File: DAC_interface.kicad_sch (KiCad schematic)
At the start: 8 parts

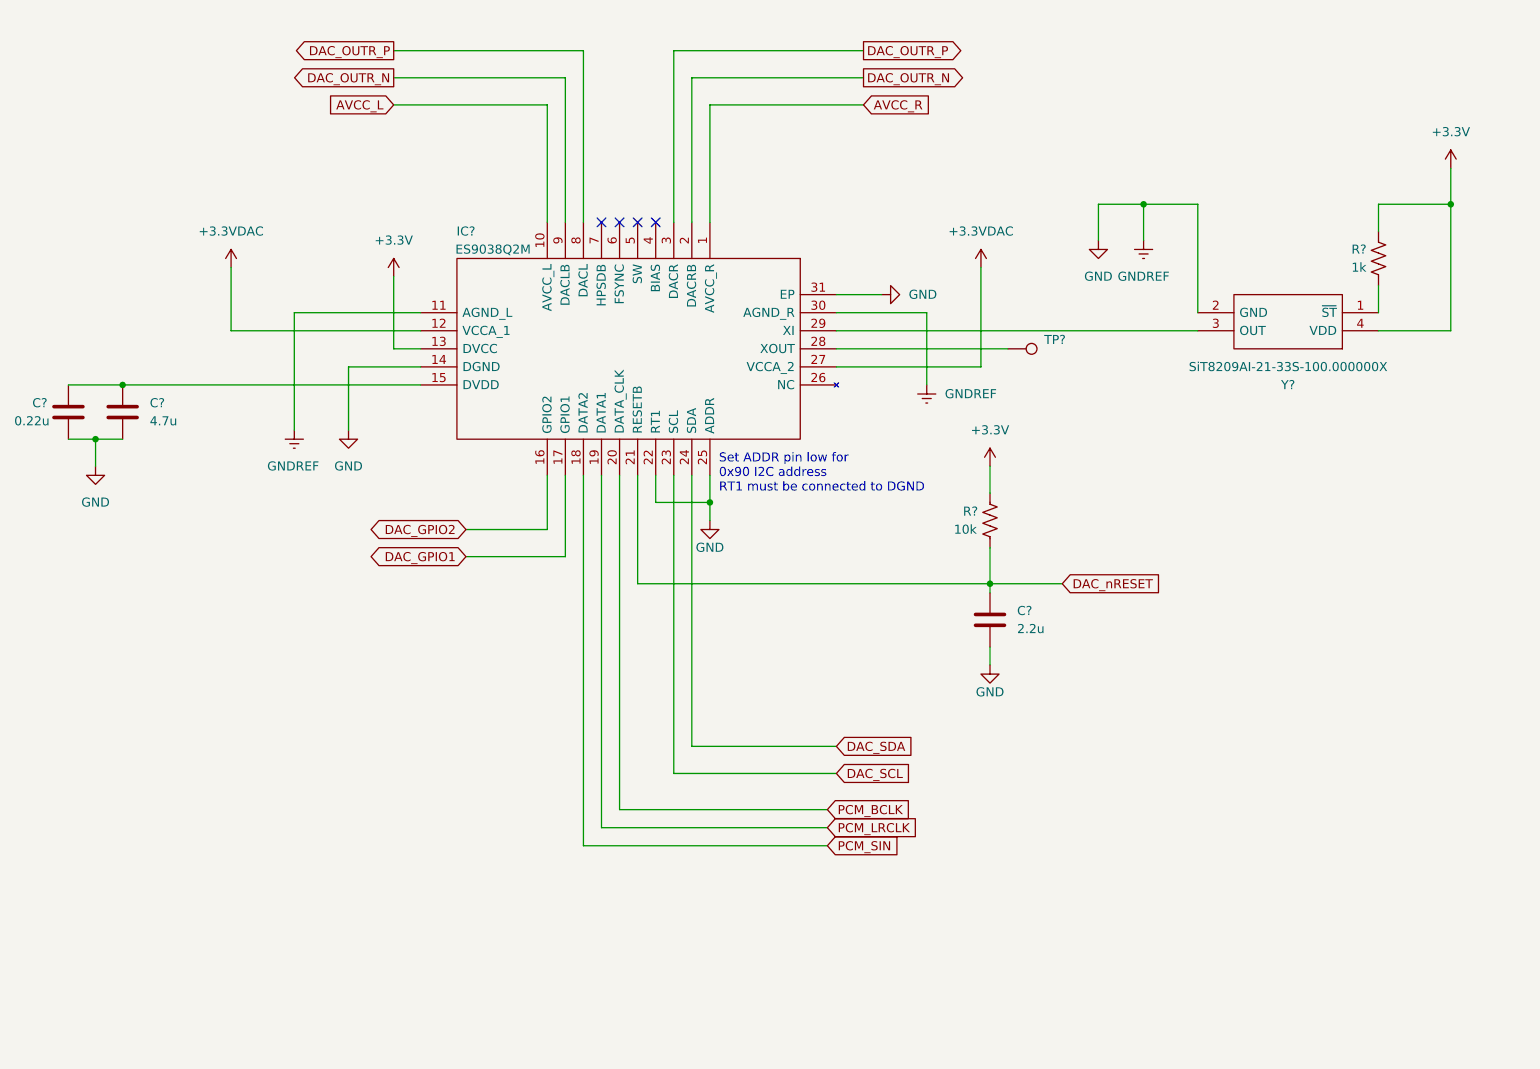
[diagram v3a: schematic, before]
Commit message: Finishing Schematic. Fixed ERC errors
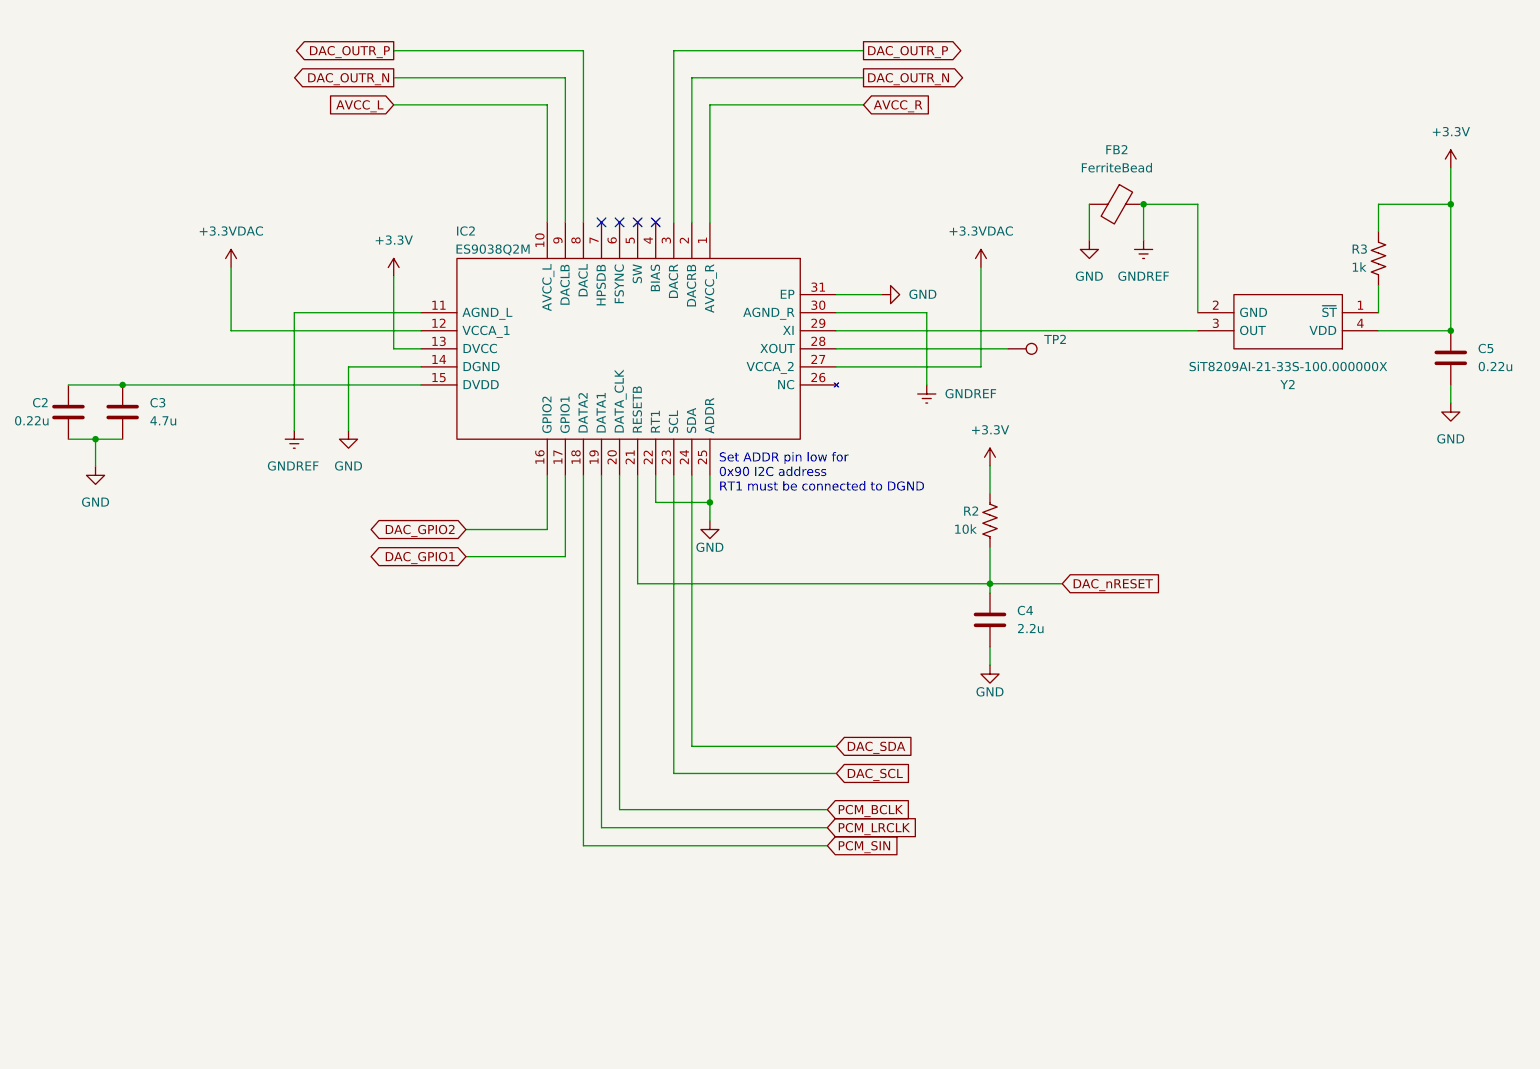
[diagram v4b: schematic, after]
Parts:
- added C5: 0.22u, symbol Device:C
- added FB2: FerriteBead, symbol Device:FerriteBead
- gave numbers to parts that had none: 8
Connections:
- net +3V3: now also C5.1
- net GND: now also C5.2, FB2.2; no longer IC2.11 (AGND_L), IC2.30 (AGND_R), Y2.2 (GND)
- new net GNDREF: FB2.1, IC2.11 (AGND_L), IC2.30 (AGND_R), Y2.2 (GND)

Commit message: Adding footprints
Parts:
- C2, C3, C4, C5: footprint (none) -> Capacitor_SMD:C_0805_2012Metric_Pad1.18x1.45mm_HandSolder
- IC2: footprint QFN40P300X500X80-31N-D -> SamacSys_Parts:QFN40P300X500X80-31N-D
- R2, R3: footprint (none) -> Resistor_SMD:R_0805_2012Metric_Pad1.20x1.40mm_HandSolder
- TP2: footprint (none) -> TestPoint:TestPoint_Pad_D2.0mm
- Y2: footprint SiT8209AI2133S100000000X -> SamacSys_Parts:SiT8209AI2133S100000000X
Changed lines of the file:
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@@
     (property "Reference" "Y2" (id 0) (at 223.52 85.09 0))
     (property "Value" "SiT8209AI-21-33S-100.000000X" (id 1) (at 223.52 82.55 0))
-    (property "Footprint" "SiT8209AI2133S100000000X" (id 2) (at 214.63 80.01 0)
+    (property "Footprint" "SamacSys_Parts:SiT8209AI2133S100000000X" (id 2) (at 214.63 80.01 0)
       (effects (font (size 1.27 1.27)) (justify left) hide)
     )
@@
       (effects (font (size 1.27 1.27)) (justify left))
     )
-    (property "Footprint" "" (id 2) (at 182.5752 121.92 0)
+    (property "Footprint" "Capacitor_SMD:C_0805_2012Metric_Pad1.18x1.45mm_HandSolder" (id 2) (at 182.5752 121.92 0)
       (effects (font (size 1.27 1.27)) hide)
     )
@@
       (effects (font (size 1.27 1.27)) (justify left))
     )
-    (property "Footprint" "" (id 2) (at 182.626 104.394 90)
+    (property "Footprint" "Resistor_SMD:R_0805_2012Metric_Pad1.20x1.40mm_HandSolder" (id 2) (at 182.626 104.394 90)
       (effects (font (size 1.27 1.27)) hide)
     )
@@
       (effects (font (size 1.27 1.27)) (justify left))
     )
-    (property "Footprint" "" (id 2) (at 247.3452 85.09 0)
+    (property "Footprint" "Capacitor_SMD:C_0805_2012Metric_Pad1.18x1.45mm_HandSolder" (id 2) (at 247.3452 85.09 0)
       (effects (font (size 1.27 1.27)) hide)
     )
@@
       (effects (font (size 1.27 1.27)) (justify left))
     )
-    (property "Footprint" "" (id 2) (at 53.0352 92.71 0)
+    (property "Footprint" "Capacitor_SMD:C_0805_2012Metric_Pad1.18x1.45mm_HandSolder" (id 2) (at 53.0352 92.71 0)
       (effects (font (size 1.27 1.27)) hide)
     )
@@
       (effects (font (size 1.27 1.27)) (justify left) hide)
     )
-    (property "Footprint" "" (id 2) (at 184.15 85.09 0)
+    (property "Footprint" "TestPoint:TestPoint_Pad_D2.0mm" (id 2) (at 184.15 85.09 0)
       (effects (font (size 1.27 1.27)) hide)
     )
@@
       (effects (font (size 1.27 1.27)) (justify left))
     )
-    (property "Footprint" "" (id 2) (at 60.6552 92.71 0)
+    (property "Footprint" "Capacitor_SMD:C_0805_2012Metric_Pad1.18x1.45mm_HandSolder" (id 2) (at 60.6552 92.71 0)
       (effects (font (size 1.27 1.27)) hide)
     )
@@
     (property "Reference" "IC2" (id 0) (at 107.95 63.5 90))
     (property "Value" "ES9038Q2M" (id 1) (at 111.76 66.04 90))
-    (property "Footprint" "QFN40P300X500X80-31N-D" (id 2) (at 154.94 93.98 0)
+    (property "Footprint" "SamacSys_Parts:QFN40P300X500X80-31N-D" (id 2) (at 154.94 93.98 0)
       (effects (font (size 1.27 1.27)) (justify left) hide)
     )
@@
       (effects (font (size 1.27 1.27)) (justify left))
     )
-    (property "Footprint" "" (id 2) (at 237.236 67.564 90)
-      (effects (font (size 1.27 1.27)) hide)
-    )
+    (property "Footprint" "Resistor_SMD:R_0805_2012Metric_Pad1.20x1.40mm_HandSolder" (id 2) (at 237.236 67.564 90)
+      (effects (font (size 1.27 1.27)) hide)
+    )
